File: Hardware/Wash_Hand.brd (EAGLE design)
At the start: 71.1 x 48.3 mm, 69 parts, among them IC1 LM358D, IC2 LP298XS, IC3 405016TSSOP, J1 I2C, J2 ICSP, J3 SPI, J4 9V_CONN, J5 EXT_VCC, J6 6_PIN_SERIAL_CABLEPTH, Q1 16.0 Mhz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

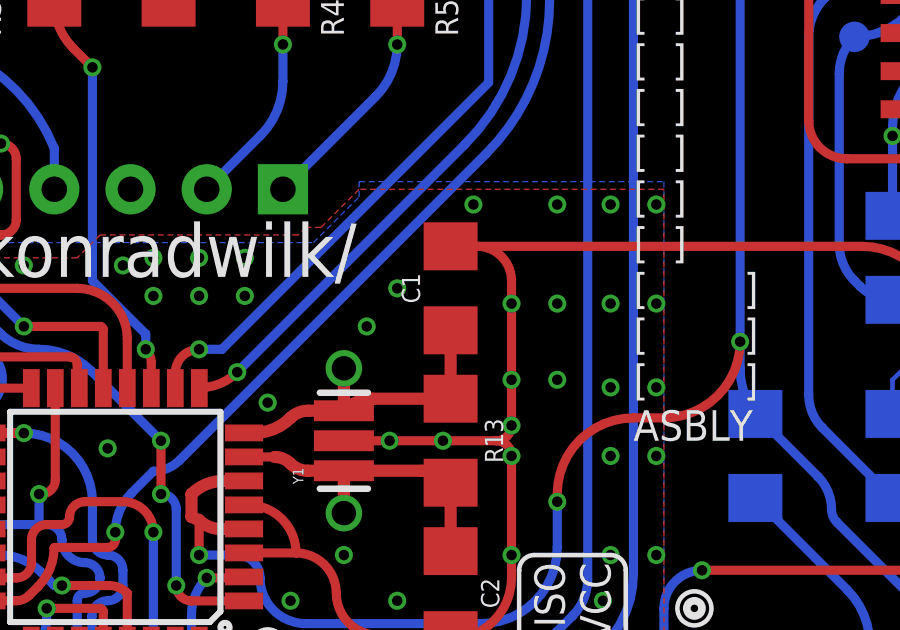
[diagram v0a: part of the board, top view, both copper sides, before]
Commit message: Board/Schematic: Name some of the line sensor
circuits parts, instead of U$1,U$2, and so on.

Signed-off-by: Konrad Rzeszutek Wilk <konrad@kernel.org>
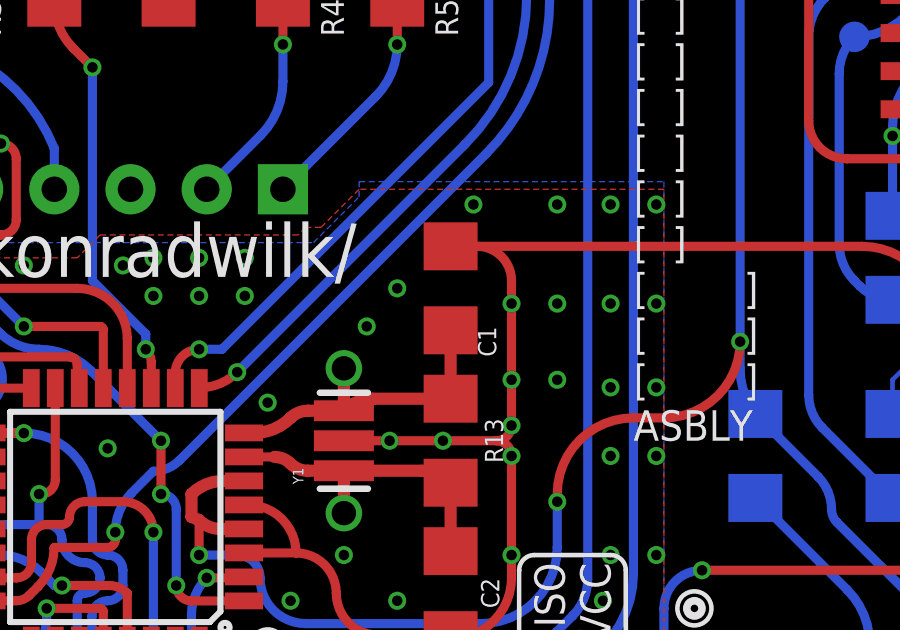
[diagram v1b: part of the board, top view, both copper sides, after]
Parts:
- renumbered U$1 to R15, U$2 to R14, U$3 to E, U$6 to D
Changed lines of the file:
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@@
 <elements>
 <element name="C1" library="SparkFun-Capacitors" library_urn="urn:adsk.eagle:library:510" package="1206" package3d_urn="urn:adsk.eagle:package:37426/1" value="10pF" x="46.736" y="20.574" smashed="yes" rot="R90">
-<attribute name="NAME" x="45.72" y="20.574" size="0.6096" layer="25" font="vector" ratio="20" rot="R90" align="bottom-center"/>
+<attribute name="NAME" x="48.26" y="18.796" size="0.6096" layer="25" font="vector" ratio="20" rot="R90" align="bottom-center"/>
 <attribute name="PROD_ID" value="CAP-10057" x="101.346" y="43.434" size="1.778" layer="27" rot="R90" display="off"/>
 <attribute name="VALUE" value="10uF" x="47.752" y="20.574" size="0.6096" layer="27" font="vector" ratio="20" rot="R90" align="top-center"/>
@@
 <attribute name="VALUE" x="68.072" y="37.4015" size="0.6096" layer="27" font="vector" ratio="20" align="top-center"/>
 </element>
-<element name="U$1" library="darnok_common" package="1206" value="10K" x="61.468" y="14.986" smashed="yes" rot="MR90">
+<element name="R15" library="darnok_common" package="1206" value="10K" x="61.468" y="14.986" smashed="yes" rot="MR90">
 <attribute name="NAME" x="62.611" y="14.986" size="0.6096" layer="26" font="vector" ratio="20" rot="MR90" align="bottom-center"/>
 <attribute name="VALUE" x="60.325" y="14.986" size="0.6096" layer="28" font="vector" ratio="20" rot="MR90" align="top-center"/>
@@
 <attribute name="VALUE" x="63.881" y="30.607" size="1.27" layer="28" rot="MR180"/>
 </element>
-<element name="U$3" library="darnok_sensors" package="LTE-302" value="LTE-302" x="68.072" y="34.544" smashed="yes" rot="MR0">
+<element name="E" library="darnok_sensors" package="LTE-302" value="LTE-302" x="68.072" y="34.544" smashed="yes" rot="MR0">
 <attribute name="NAME" x="70.358" y="34.544" size="0.6096" layer="26" font="vector" ratio="20" rot="MR90" align="bottom-center"/>
 <attribute name="VALUE" x="65.786" y="34.544" size="0.6096" layer="28" font="vector" ratio="20" rot="MR90" align="top-center"/>
 </element>
-<element name="U$6" library="darnok_sensors" package="LTR-301" value="LTR-301" x="62.23" y="34.544" smashed="yes" rot="MR0">
+<element name="D" library="darnok_sensors" package="LTR-301" value="LTR-301" x="62.23" y="34.544" smashed="yes" rot="MR0">
 <attribute name="NAME" x="64.516" y="34.544" size="0.6096" layer="26" font="vector" ratio="20" rot="MR90" align="bottom-center"/>
 <attribute name="VALUE" x="59.944" y="34.544" size="0.6096" layer="28" font="vector" ratio="20" rot="MR90" align="top-center"/>
 </element>
-<element name="U$2" library="darnok_common" package="1206" value="220" x="61.468" y="21.59" smashed="yes" rot="MR90">
+<element name="R14" library="darnok_common" package="1206" value="220" x="61.468" y="21.59" smashed="yes" rot="MR90">
 <attribute name="NAME" x="62.611" y="21.59" size="0.6096" layer="26" font="vector" ratio="20" rot="MR90" align="bottom-center"/>
 <attribute name="VALUE" x="60.325" y="21.59" size="0.6096" layer="28" font="vector" ratio="20" rot="MR90" align="top-center"/>
@@
 <contactref element="J4" pad="2"/>
 <contactref element="TM1" pad="1"/>
-<contactref element="U$3" pad="C"/>
-<contactref element="U$6" pad="E"/>
+<contactref element="E" pad="C"/>
+<contactref element="D" pad="E"/>
 <contactref element="J2" pad="6"/>
 <contactref element="IC2" pad="2"/>
@@
 <signal name="N$15">
 <contactref element="JP4" pad="2"/>
-<contactref element="U$1" pad="2"/>
+<contactref element="R15" pad="2"/>
 <contactref element="TM1" pad="3"/>
-<contactref element="U$2" pad="2"/>
+<contactref element="R14" pad="2"/>
 <wire x1="62.169" y1="22.99" x2="61.468" y2="22.99" width="0.1524" layer="16"/>
 <wire x1="61.468" y1="16.386" x2="61.468" y2="17.526" width="0.1524" layer="16"/>
@@
 <signal name="N$14">
 <contactref element="IC1" pad="3"/>
-<contactref element="U$6" pad="C"/>
-<contactref element="U$1" pad="1"/>
+<contactref element="D" pad="C"/>
+<contactref element="R15" pad="1"/>
 <contactref element="TP3" pad="P$1"/>
 <via x="64.008" y="33.02" extent="1-16" drill="0.35"/>
@@
 </signal>
 <signal name="N$11">
-<contactref element="U$2" pad="1"/>
-<contactref element="U$3" pad="A"/>
+<contactref element="R14" pad="1"/>
+<contactref element="E" pad="A"/>
 <contactref element="TP4" pad="P$1"/>
 <wire x1="66.802" y1="34.544" x2="61.932421875" y2="29.674421875" width="0.3048" layer="16"/>

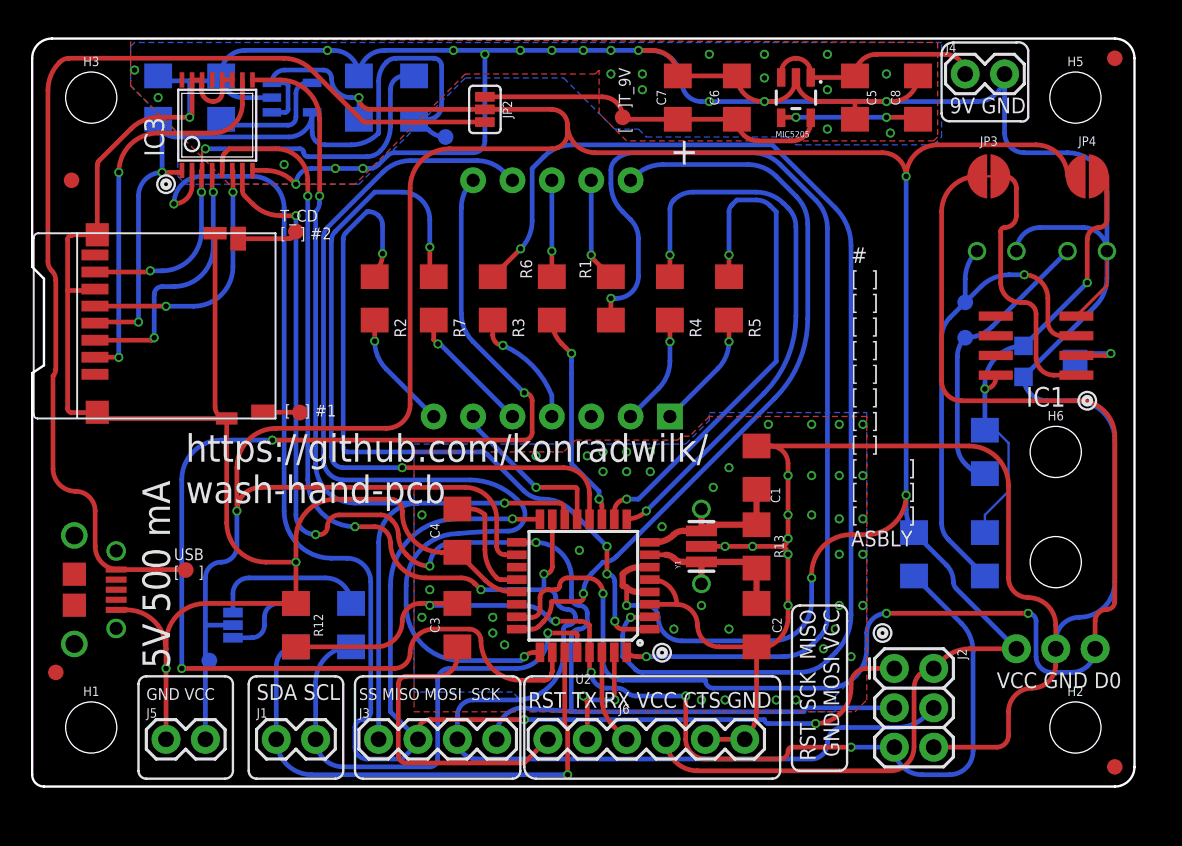
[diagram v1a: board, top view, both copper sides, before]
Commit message: Board: Add USB ground plane.
And connect it with the other two.

Signed-off-by: Konrad Rzeszutek Wilk <konrad@kernel.org>
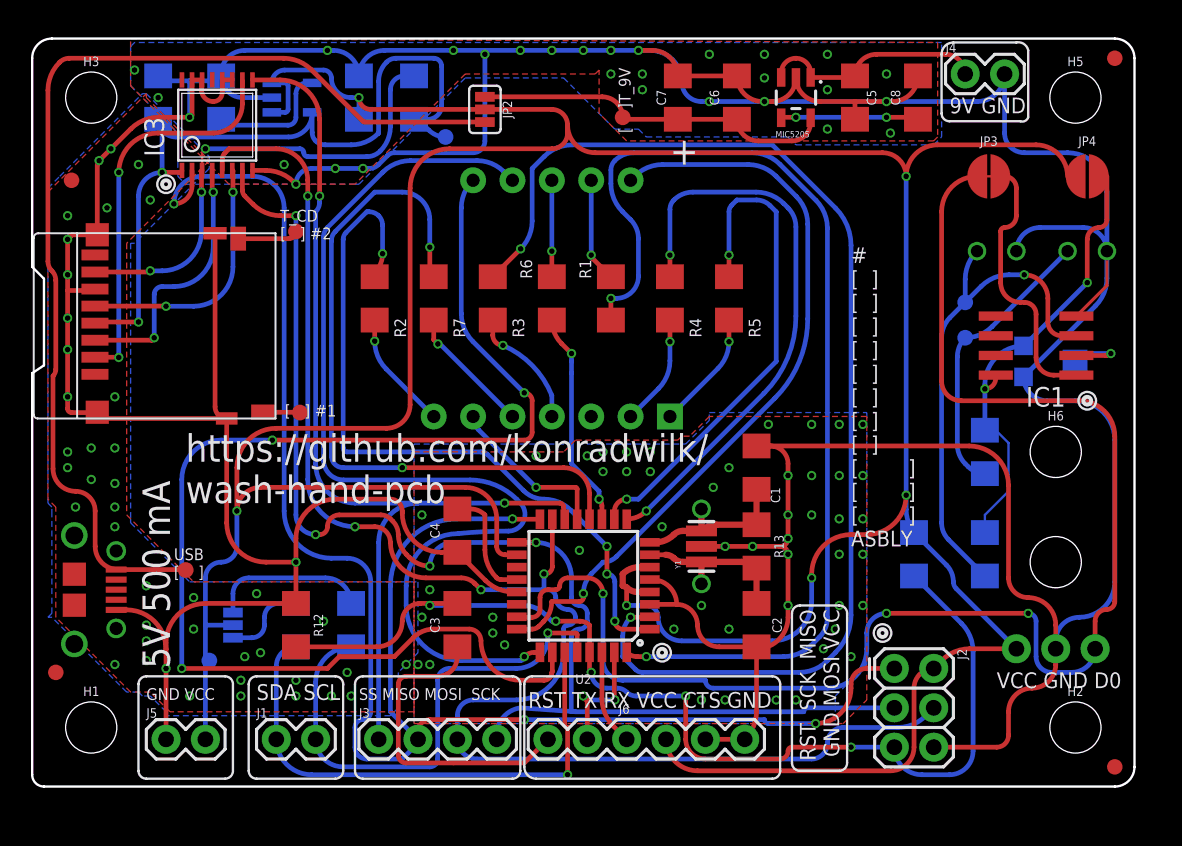
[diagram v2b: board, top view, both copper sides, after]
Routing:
- net 0: vias 78 -> 121
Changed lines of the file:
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@@
 <wire x1="2.286" y1="24.384" x2="2.54" y2="24.13" width="0.3048" layer="1" curve="90"/>
 <wire x1="2.54" y1="24.13" x2="4.182" y2="24.13" width="0.3048" layer="1"/>
-<wire x1="2.286" y1="35.306" x2="2.286" y2="32.004" width="0.3048" layer="1"/>
-<wire x1="2.286" y1="32.004" x2="2.286" y2="24.384" width="0.3048" layer="1"/>
+<wire x1="2.286" y1="35.306" x2="2.286" y2="33.02" width="0.3048" layer="1"/>
+<wire x1="2.286" y1="33.02" x2="2.286" y2="32.004" width="0.3048" layer="1"/>
+<wire x1="2.286" y1="32.004" x2="2.286" y2="30.226" width="0.3048" layer="1"/>
+<wire x1="2.286" y1="30.226" x2="2.286" y2="28.194" width="0.3048" layer="1"/>
+<wire x1="2.286" y1="28.194" x2="2.286" y2="25.146" width="0.3048" layer="1"/>
+<wire x1="2.286" y1="25.146" x2="2.286" y2="24.384" width="0.3048" layer="1"/>
 <wire x1="4.05" y1="32.098" x2="3.956" y2="32.004" width="0.3048" layer="1" curve="-90"/>
 <wire x1="3.956" y1="32.004" x2="2.286" y2="32.004" width="0.3048" layer="1"/>
@@
 <wire x1="4.2" y1="35.598" x2="4.2" y2="40.101121875" width="0.3048" layer="1"/>
 <wire x1="4.2" y1="40.101121875" x2="4.318" y2="40.386" width="0.3048" layer="1" curve="-45"/>
-<wire x1="4.318" y1="40.386" x2="6.36805" y2="42.43605" width="0.3048" layer="1"/>
+<wire x1="4.318" y1="40.386" x2="5.08" y2="41.148" width="0.3048" layer="1"/>
+<wire x1="5.08" y1="41.148" x2="6.36805" y2="42.43605" width="0.3048" layer="1"/>
 <wire x1="6.36805" y1="42.43605" x2="8.164103125" y2="43.18" width="0.3048" layer="1" curve="-45"/>
 <wire x1="8.164103125" y1="43.18" x2="10.16" y2="43.18" width="0.3048" layer="1"/>
@@
 <vertex x="34.29" y="21.59"/>
 <vertex x="24.638" y="21.59"/>
-<vertex x="24.638" y="4.826"/>
-<vertex x="53.086" y="4.826"/>
+<vertex x="24.638" y="4.064"/>
+<vertex x="52.324" y="4.064"/>
 <vertex x="53.848" y="5.588"/>
 </polygon>
@@
 <vertex x="53.848" y="7.874"/>
 <vertex x="51.816" y="5.842"/>
-<vertex x="51.816" y="4.826"/>
-<vertex x="32.258" y="4.826"/>
-<vertex x="30.988" y="6.096"/>
-<vertex x="24.638" y="6.096"/>
+<vertex x="51.816" y="4.064"/>
+<vertex x="24.638" y="4.064"/>
 <vertex x="24.638" y="22.098"/>
 <vertex x="42.164" y="22.098"/>
@@
 <via x="35.56" y="47.498" extent="1-16" drill="0.35"/>
 <via x="31.496" y="47.498" extent="1-16" drill="0.35"/>
+<polygon width="0.1524" layer="1">
+<vertex x="24.638" y="4.826"/>
+<vertex x="8.89" y="4.826"/>
+<vertex x="7.62" y="6.096"/>
+<vertex x="6.35" y="6.096"/>
+<vertex x="1.524" y="10.922"/>
+<vertex x="1.524" y="18.034"/>
+<vertex x="1.016" y="18.542"/>
+<vertex x="1.016" y="38.354"/>
+<vertex x="7.366" y="44.704"/>
+<vertex x="7.366" y="44.45"/>
+<vertex x="11.43" y="40.386"/>
+<vertex x="6.096" y="35.052"/>
+<vertex x="6.096" y="33.02"/>
+<vertex x="6.096" y="17.526"/>
+<vertex x="7.874" y="15.748"/>
+<vertex x="10.414" y="13.208"/>
+<vertex x="24.638" y="13.208"/>
+</polygon>
+<polygon width="0.1524" layer="16">
+<vertex x="8.636" y="4.826"/>
+<vertex x="7.62" y="5.842"/>
+<vertex x="7.112" y="5.842"/>
+<vertex x="6.858" y="6.096"/>
+<vertex x="6.096" y="6.096"/>
+<vertex x="1.27" y="10.922"/>
+<vertex x="1.016" y="10.922"/>
+<vertex x="1.27" y="11.176"/>
+<vertex x="1.27" y="17.526"/>
+<vertex x="1.27" y="18.034"/>
+<vertex x="1.016" y="18.288"/>
+<vertex x="1.016" y="38.608"/>
+<vertex x="1.778" y="39.37"/>
+<vertex x="7.112" y="44.704"/>
+<vertex x="7.366" y="44.704"/>
+<vertex x="11.43" y="40.64"/>
+<vertex x="11.43" y="39.878"/>
+<vertex x="6.604" y="35.052"/>
+<vertex x="6.35" y="35.052"/>
+<vertex x="6.35" y="17.272"/>
+<vertex x="6.35" y="17.018"/>
+<vertex x="10.16" y="13.208"/>
+<vertex x="24.892" y="13.208"/>
+<vertex x="24.892" y="8.636"/>
+<vertex x="23.622" y="7.366"/>
+<vertex x="23.622" y="5.08"/>
+<vertex x="23.114" y="4.572"/>
+<vertex x="8.636" y="4.572"/>
+</polygon>
+<via x="2.286" y="25.146" extent="1-16" drill="0.35"/>
+<via x="2.286" y="28.194" extent="1-16" drill="0.35"/>
+<via x="2.286" y="30.226" extent="1-16" drill="0.35"/>
+<via x="2.286" y="33.02" extent="1-16" drill="0.35"/>
+<via x="2.286" y="35.306" extent="1-16" drill="0.35"/>
+<via x="4.318" y="40.386" extent="1-16" drill="0.35"/>
+<via x="5.08" y="41.148" extent="1-16" drill="0.35"/>
+<via x="4.826" y="37.338" extent="1-16" drill="0.35"/>
+<via x="2.286" y="36.83" extent="1-16" drill="0.35"/>
+<via x="6.858" y="40.132" extent="1-16" drill="0.35"/>
+<via x="7.62" y="37.846" extent="1-16" drill="0.35"/>
+<via x="5.334" y="25.146" extent="1-16" drill="0.35"/>
+<via x="5.334" y="21.844" extent="1-16" drill="0.35"/>
+<via x="3.81" y="21.844" extent="1-16" drill="0.35"/>
+<via x="2.286" y="21.59" extent="1-16" drill="0.35"/>
+<via x="3.81" y="19.812" extent="1-16" drill="0.35"/>
+<via x="5.334" y="19.558" extent="1-16" drill="0.35"/>
+<via x="5.334" y="18.034" extent="1-16" drill="0.35"/>
+<via x="5.334" y="16.764" extent="1-16" drill="0.35"/>
+<via x="7.366" y="12.954" extent="1-16" drill="0.35"/>
+<via x="10.414" y="12.192" extent="1-16" drill="0.35"/>
+<via x="14.478" y="12.446" extent="1-16" drill="0.35"/>
+<via x="14.732" y="8.636" extent="1-16" drill="0.35"/>
+<via x="7.366" y="10.414" extent="1-16" drill="0.35"/>
+<via x="5.334" y="7.874" extent="1-16" drill="0.35"/>
+<via x="7.366" y="8.128" extent="1-16" drill="0.35"/>
+<via x="10.16" y="5.842" extent="1-16" drill="0.35"/>
+<via x="7.366" y="9.398" extent="1-16" drill="0.35"/>
+<via x="18.796" y="10.668" extent="1-16" drill="0.35"/>
+<via x="19.304" y="5.842" extent="1-16" drill="0.35"/>
+<via x="20.574" y="5.842" extent="1-16" drill="0.35"/>
+<via x="17.018" y="5.842" extent="1-16" drill="0.35"/>
+<via x="13.462" y="5.842" extent="1-16" drill="0.35"/>
+<via x="10.414" y="10.16" extent="1-16" drill="0.35"/>
+<via x="2.286" y="20.574" extent="1-16" drill="0.35"/>
+<via x="2.794" y="18.034" extent="1-16" drill="0.35"/>
+<via x="13.716" y="8.382" extent="1-16" drill="0.35"/>
+<via x="24.892" y="7.874" extent="1-16" drill="0.35"/>
+<via x="25.654" y="7.874" extent="1-16" drill="0.35"/>
+<via x="20.32" y="7.366" extent="1-16" drill="0.35"/>
+<via x="24.13" y="7.874" extent="1-16" drill="0.35"/>
+<via x="13.462" y="6.858" extent="1-16" drill="0.35"/>
+<via x="17.018" y="6.858" extent="1-16" drill="0.35"/>
 </signal>
 <signal name="D0">
@@
 <wire x1="28.956" y1="9.398" x2="28.194" y2="10.16" width="0.3048" layer="1" curve="90"/>
 <wire x1="28.194" y1="10.16" x2="25.908" y2="10.16" width="0.3048" layer="1"/>
-<wire x1="25.908" y1="10.16" x2="24.384" y2="8.636" width="0.3048" layer="1" curve="90"/>
-<wire x1="24.384" y1="8.636" x2="23.368" y2="7.62" width="0.3048" layer="1" curve="-90"/>
-<wire x1="23.368" y1="7.62" x2="9.652" y2="7.62" width="0.3048" layer="1"/>
 <via x="9.652" y="7.62" extent="1-16" drill="0.35"/>
 <wire x1="9.652" y1="7.62" x2="9.652" y2="19.812" width="0.3048" layer="16"/>
@@
 <wire x1="32.258" y1="22.86" x2="32.258" y2="24.892" width="0.3048" layer="1"/>
 <wire x1="28.42995" y1="28.72005" x2="31.75" y2="25.4" width="0.3048" layer="16"/>
+<wire x1="9.652" y1="7.62" x2="19.05" y2="7.62" width="0.3048" layer="1"/>
+<wire x1="19.05" y1="7.62" x2="19.812" y2="8.382" width="0.3048" layer="1"/>
+<wire x1="19.812" y1="8.382" x2="23.368" y2="8.382" width="0.3048" layer="1"/>
+<wire x1="23.368" y1="8.382" x2="24.607184375" y2="9.621184375" width="0.3048" layer="1"/>
+<wire x1="24.607184375" y1="9.621184375" x2="25.908" y2="10.16" width="0.3048" layer="1" curve="-45"/>
 </signal>
 <signal name="D2">

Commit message: Board/Schedule: Add 1K and LED on SCK line.
Signed-off-by: Konrad Rzeszutek Wilk <konrad@kernel.org>
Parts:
- added LED1: RED, adafruit:1206
- added R16: 1K, darnok_common:1206
- moved R12 4.06 mm to (13.0, 10.4)
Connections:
- new net N$7: LED1.C, R16.1
- net 0: now also LED1.A
- net SCK: now also R16.2
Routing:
- net SCK: track 85.6 -> 91.0 mm
- net RESET: track 68.3 -> 72.5 mm
- net N$7: track 0.00 -> 3.57 mm
- net 0: track 361.7 -> 362.7 mm, vias 121 -> 123

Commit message: Board/Schematic: Update RELEASE to be main
As that is the current release train.

Signed-off-by: Konrad Rzeszutek Wilk <konrad@kernel.org>
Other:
- board text added: "main"
- board text removed: "v1.3b.rc4"
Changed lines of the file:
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@@
 <circle x="8.636" y="38.862" radius="0.254" width="0.254" layer="25"/>
 <circle x="8.636" y="38.862" radius="0.567959375" width="0.1524" layer="25"/>
-<text x="32.004" y="5.842" size="1.778" layer="26" ratio="14" rot="MR0">v1.3b.rc4</text>
+<text x="32.004" y="5.842" size="1.778" layer="26" ratio="14" rot="MR0">main</text>
 <text x="52.832" y="15.494" size="1.016" layer="25" ratio="14">#
 [  ]
